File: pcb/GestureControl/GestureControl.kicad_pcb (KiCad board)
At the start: 4 copper layers, 253.9 x 54.6 mm, 177 parts, among them J1 Conn_01x04_I2I-LCD, J10 EXTERN I2C, J11 Conn_01x02, J12 Conn_01x02, J13 WR-MM Female SMT Connector, J14 WR-MM Female SMT Connector, J15 WR-MM Female SMT Connector, J16 WR-MM Female SMT Connector, J17 Conn_01x01, J18 Conn_01x01, J19 Conn_01x01, J2 BATT, J20 WR-MM Female SMT Connector, J21 WR-MM Female SMT Connector, J22 WR-MM Female SMT Connector, J23 WR-MM Female SMT Connector, J3 Conn_01x08, J4 Conn_01x06, J5 Conn_01x10, J6 Conn_01x08, J7 FTDI, J8 Conn_01x06, J9 UART, SW1 SW1, SW2 SW2, U1 AP5100_3.3, U2 AP5100_3.3, U3 VL53L3CXV0DH_1, U4 VL53L3CXV0DH_1, U5 VL53L3CXV0DH_1, U6 STM32L151RETx, U7 STM32F401RETx, U8 VL53L3CXV0DH_1, U9 VL53L3CXV0DH_1, Y1 8MHz, Y2 32kHz

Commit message: small change
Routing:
- net GND: track 427.3 -> 424.8 mm
- net +5V: track 112.6 -> 112.1 mm
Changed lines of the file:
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@@
     (effects (font (size 1 1) (thickness 0.2)) (justify left))
   )
-  (gr_text "I2C LCD" (at 40.132 96.774) (layer "F.SilkS")
+  (gr_text "I2C LCD" (at 38.1 96.774) (layer "F.SilkS")
     (effects (font (size 1 1) (thickness 0.2)))
   )
@@
     (effects (font (size 1 1) (thickness 0.2)) (justify left))
   )
-  (gr_text "FTDI" (at 41.656 88.9) (layer "F.SilkS")
+  (gr_text "FTDI" (at 42.799 86.741) (layer "F.SilkS")
     (effects (font (size 1 1) (thickness 0.2)))
   )
@@
   (segment (start 117.856 91.694) (end 116.332 91.694) (width 1) (layer "B.Cu") (net 1))
   (segment (start 104.648 88.809) (end 104.648 90.73292) (width 0.25) (layer "B.Cu") (net 1))
-  (segment (start 60.06549 88.38649) (end 58.28749 88.38649) (width 0.25) (layer "B.Cu") (net 1))
   (segment (start 68.99849 100.57849) (end 68.95549 100.57849) (width 0.25) (layer "B.Cu") (net 1))
   (segment (start 60.06549 88.38649) (end 60.06549 87.24349) (width 0.25) (layer "B.Cu") (net 1))
@@
   (segment (start 215.392 98.425) (end 214.122 98.425) (width 0.25) (layer "B.Cu") (net 1))
   (segment (start 132.588 92.379) (end 134.0565 92.379) (width 1) (layer "B.Cu") (net 1))
-  (segment (start 58.28749 88.38649) (end 57.77949 88.89449) (width 0.25) (layer "B.Cu") (net 1))
   (segment (start 253.492 98.425) (end 253.492 97.331) (width 0.25) (layer "B.Cu") (net 1))
   (segment (start 255.107 102.906) (end 256.413 102.906) (width 0.5) (layer "B.Cu") (net 1))
@@
   (segment (start 37.592 93.726) (end 37.592 89.535) (width 1) (layer "In2.Cu") (net 21))
   (segment (start 37.592 99.187) (end 37.592 99.314) (width 1) (layer "In2.Cu") (net 21))
-  (segment (start 37.592 93.726) (end 37.592 93.218) (width 1) (layer "In2.Cu") (net 21))
   (segment (start 37.592 98.425) (end 38.354 98.425) (width 1) (layer "In2.Cu") (net 21))
   (segment (start 54.584489 125.501511) (end 56.134 123.952) (width 1) (layer "In2.Cu") (net 21))
@@
   (segment (start 110.454717 107.097) (end 109.728 107.097) (width 0.25) (layer "B.Cu") (net 33))
   (segment (start 43.053 79.375) (end 43.053 85.09) (width 0.25) (layer "B.Cu") (net 33))
-  (segment (start 43.053 85.09) (end 43.033501 85.109499) (width 0.25) (layer "B.Cu") (net 33))
   (segment (start 108.458 83.657) (end 108.458 93.309) (width 0.25) (layer "B.Cu") (net 33))
   (segment (start 260.223 107.533) (end 260.223 109.3978) (width 0.25) (layer "B.Cu") (net 33))
@@
   (segment (start 184.023 109.347) (end 186.944 112.268) (width 0.25) (layer "B.Cu") (net 33))
   (segment (start 108.458 108.93) (end 108.458 119.725) (width 0.25) (layer "B.Cu") (net 33))
-  (segment (start 45.244078 96.51449) (end 45.07949 96.51449) (width 0.25) (layer "B.Cu") (net 33))
   (segment (start 61.11749 93.12549) (end 61.11749 98.00249) (width 0.25) (layer "F.Cu") (net 34))
   (segment (start 43.121478 88.89449) (end 45.154467 90.927479) (width 0.25) (layer "F.Cu") (net 34))
@@
   (segment (start 52.95349 94.483488) (end 47.366488 94.483488) (width 0.25) (layer "F.Cu") (net 38))
   (segment (start 47.36549 94.48249) (end 44.31749 94.48249) (width 0.25) (layer "F.Cu") (net 38))
-  (segment (start 52.95349 94.483488) (end 52.95349 94.48249) (width 0.25) (layer "F.Cu") (net 38))
   (segment (start 57.69249 98.05049) (end 56.520492 98.05049) (width 0.25) (layer "F.Cu") (net 38))
   (segment (start 56.520492 98.05049) (end 52.95349 94.483488) (width 0.25) (layer "F.Cu") (net 38))
@@
   (segment (start 47.366488 94.483488) (end 47.36549 94.48249) (width 0.25) (layer "F.Cu") (net 38))
   (segment (start 57.69249 95.05049) (end 55.04549 95.05049) (width 0.25) (layer "F.Cu") (net 39))
-  (segment (start 52.954488 92.70449) (end 52.69949 92.70449) (width 0.25) (layer "F.Cu") (net 39))
   (segment (start 55.04549 95.05049) (end 52.69949 92.70449) (width 0.25) (layer "F.Cu") (net 39))
   (segment (start 57.651991 92.836031) (end 59.49147 94.67551) (width 0.25) (layer "F.Cu") (net 40))

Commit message: feedback verwerking philip
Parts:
- C29, R20: moved to F.Cu
- moved C7 13.1 mm to (23.7, 120.2), turned to 90 degrees
- moved D7 11.2 mm to (36.2, 118.4), turned to 90 degrees
- moved D8 10.3 mm to (27.4, 77.2), turned to 90 degrees
- moved R27 9.74 mm to (29.0, 113.3), turned to 90 degrees
- moved R18 9.39 mm to (24.6, 113.3), turned to -90 degrees
- moved R25 8.62 mm to (26.8, 113.3), turned to 90 degrees
- moved C5 7.63 mm to (33.3, 115.5), turned to 90 degrees
- moved C3 7.03 mm to (30.9, 124.0), turned to -90 degrees
- moved L1 6.55 mm to (40.9, 117.6), turned to 90 degrees
- moved C34 6.38 mm to (23.0, 75.1)
- moved R20 6.13 mm to (49.8, 99.6), turned to 0 degrees
- moved C13 5.95 mm to (37.0, 112.4)
- moved R23 5.69 mm to (33.3, 119.3), turned to 90 degrees
- moved C33 5.69 mm to (64.0, 99.1), turned to 180 degrees
- moved JP3 5.25 mm to (66.4, 95.5)
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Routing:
- net GND: track 424.8 -> 320.1 mm, vias 141 -> 154
- net +3V3: track 891.3 -> 869.4 mm, vias 49 -> 50
- net VCC: track 60.6 -> 50.0 mm
- net +5V: track 112.1 -> 101.9 mm, vias 5 -> 4
- net /STM32L151RET6TR/FTDI_RTS: track 33.8 -> 24.3 mm, vias 2 -> 0
- net /STM32L151RET6TR/PIN30: track 10.4 -> 2.85 mm
- net BUCK_5_EN: track 55.2 -> 48.8 mm
- net XSHUT_4: track 276.1 -> 273.3 mm
- net SDA2: track 39.3 -> 36.6 mm
- net /STM32L151RET6TR/PIN41: track 3.95 -> 6.63 mm
- net GPIOI_3: track 282.0 -> 284.3 mm
- net LED_1: track 54.9 -> 52.7 mm
- net BUCK_33_EN: track 1.98 -> 3.07 mm
- net LED_3: track 41.3 -> 40.4 mm
- net XSHUT_0: track 95.3 -> 94.4 mm
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- removed copper zone on In2.Cu, net +5V
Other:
- outline, holes or cut-outs redrawn

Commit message: feedback verwerling philip
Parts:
- C1, C2, R8, R9: moved to F.Cu
- moved R18 15.6 mm to (40.1, 115.0), turned to 180 degrees
- moved C13 15.3 mm to (23.5, 119.7), turned to 90 degrees
- moved R25 13.3 mm to (40.1, 113.0), turned to 0 degrees
- moved R8 12.7 mm to (89.5, 86.0)
- moved R14 11.9 mm to (30.5, 111.6), turned to 0 degrees
- moved L1 11.8 mm to (30.2, 122.6), turned to 180 degrees
- moved R27 11.4 mm to (40.1, 111.0), turned to 0 degrees
- moved C7 10.8 mm to (25.0, 109.5), turned to 180 degrees
- moved R6 10.4 mm to (88.7, 82.9), turned to 180 degrees
- moved C3 10.3 mm to (27.1, 114.4), turned to 180 degrees
- moved C1 8.75 mm to (87.6, 85.8)
- moved D7 6.80 mm to (29.4, 118.0), turned to 180 degrees
- moved R7 6.63 mm to (71.3, 82.9)
- moved U1 5.05 mm to (33.6, 114.4), turned to 180 degrees
- moved C5 4.40 mm to (37.4, 117.0)
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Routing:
- net VCC: track 50.0 -> 42.2 mm, vias 8 -> 0
- net +3V3: track 869.4 -> 873.5 mm, vias 50 -> 55
- net /OUT3.3: track 0.00 -> 2.70 mm
- net +5V: track 101.9 -> 99.4 mm, vias 4 -> 7
- net SW_2: track 69.3 -> 71.7 mm
- net Net-(D6-Pad2): track 4.86 -> 7.21 mm
- net GPIOI_3: track 284.3 -> 282.0 mm, vias 9 -> 7
- net SW_1: track 77.1 -> 78.6 mm
- net Net-(R25-Pad1): track 4.59 -> 5.67 mm
- net GPIOI_2: track 192.2 -> 191.2 mm
- net BUCK_33_EN: track 3.07 -> 2.01 mm
- net LED_1: track 52.7 -> 51.7 mm
- net GPIOI_1: track 142.6 -> 141.6 mm, vias 6 -> 5
- net LED_3: track 40.4 -> 39.6 mm
- net GPIOI_0: track 83.0 -> 83.8 mm
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- added copper zone on B.Cu, net GND
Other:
- board text added: "1"
- board text added: "2"
- board text added: "3"
- board text added: "4"

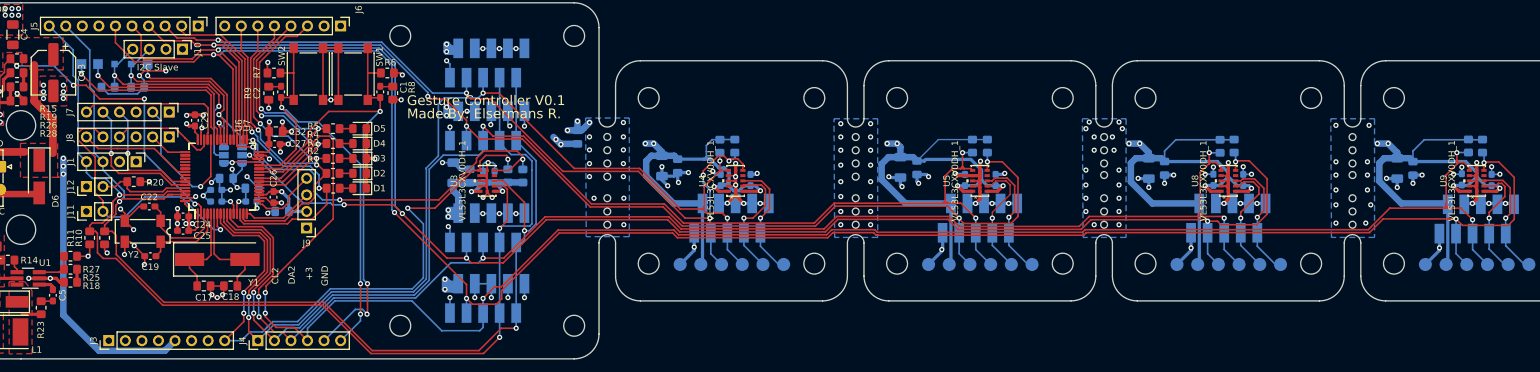
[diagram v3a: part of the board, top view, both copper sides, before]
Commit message: add vias
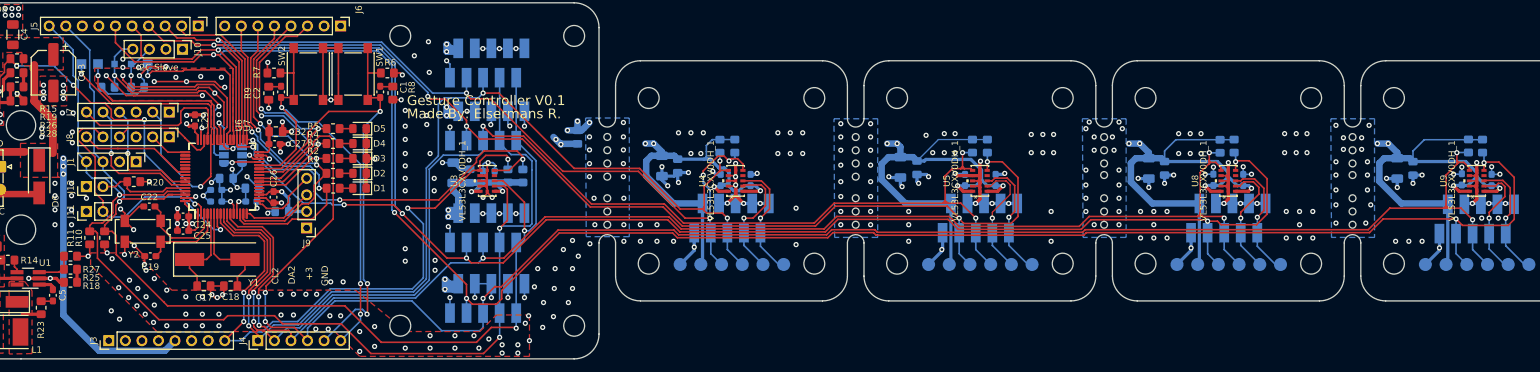
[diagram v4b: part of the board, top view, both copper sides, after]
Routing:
- net GND: track 319.4 -> 378.5 mm, vias 203 -> 393
- net /STM32L151RET6TR/PC8: track 22.1 -> 25.2 mm
- net /STM32L151RET6TR/FTDI_RTS: track 24.3 -> 26.4 mm
- net XSHUT_3: track 208.9 -> 210.3 mm
- net SDA2: track 36.6 -> 35.1 mm
- net BUCK_5_EN: track 48.8 -> 47.7 mm
- net /STM32L151RET6TR/PA10: track 29.8 -> 28.7 mm
- net SCL1: track 421.6 -> 422.6 mm
- net XSHUT_2: track 191.8 -> 192.4 mm
- added copper zone on In2.Cu, net GND

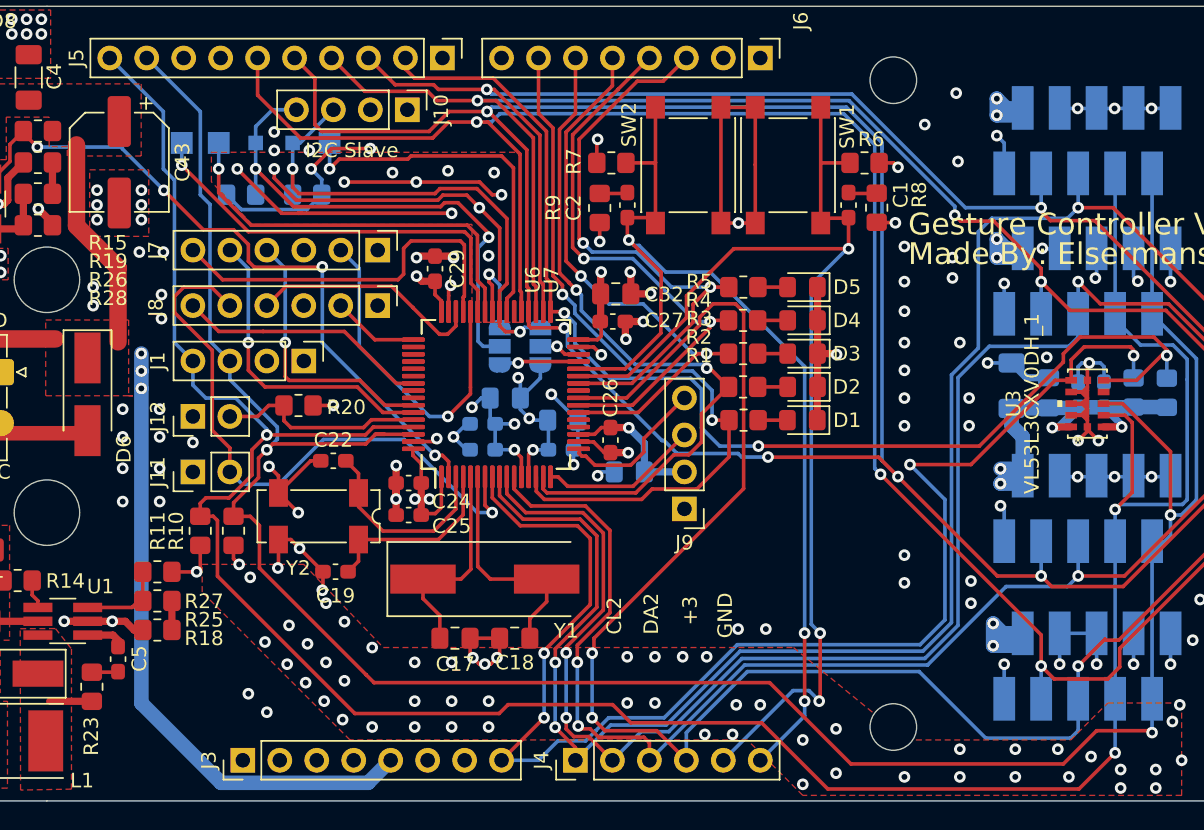
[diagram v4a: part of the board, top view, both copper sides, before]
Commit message: ADD RC op I2C
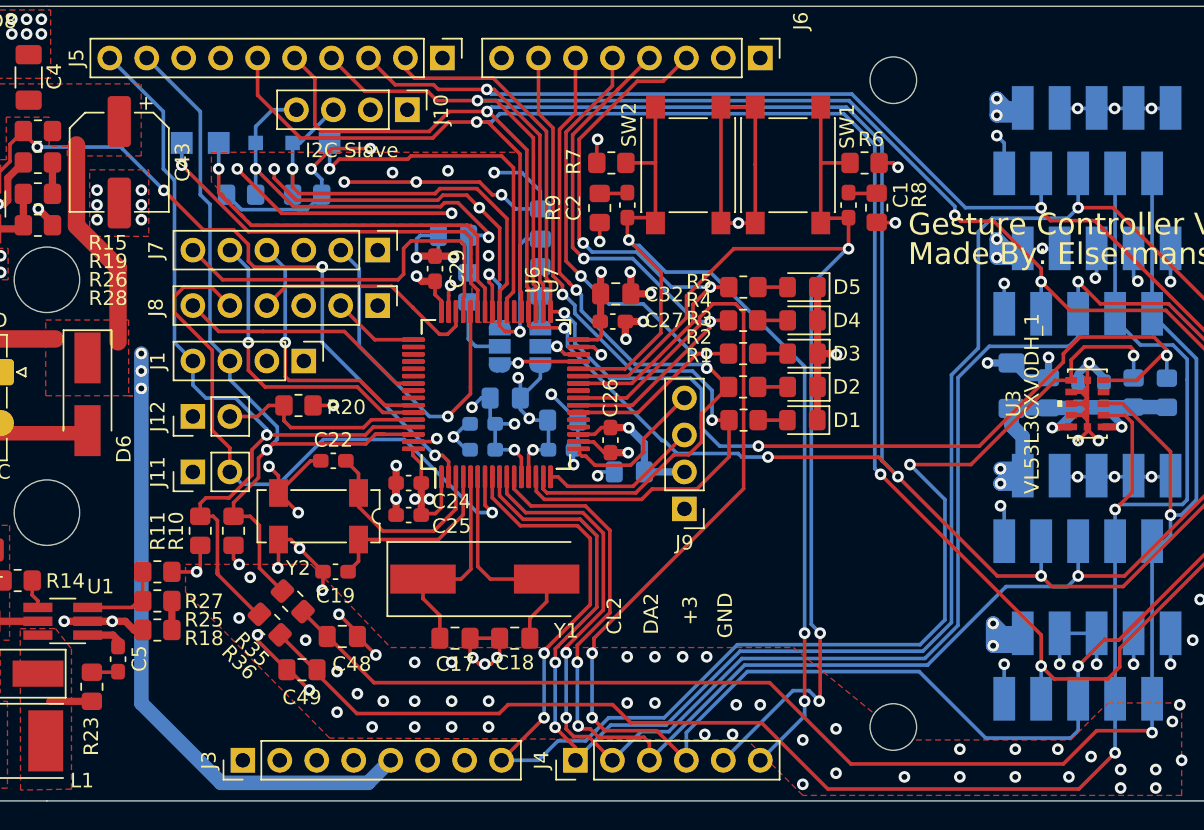
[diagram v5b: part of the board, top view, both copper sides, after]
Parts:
- added C48: x, Capacitor_SMD:C_0805_2012Metric_Pad1.18x1.45mm_HandSolder, F.Cu at (52.8, 115.4)
- added C49: x, Capacitor_SMD:C_0805_2012Metric_Pad1.18x1.45mm_HandSolder, F.Cu at (50.0, 117.7)
- added C50: x, Capacitor_SMD:C_0805_2012Metric_Pad1.18x1.45mm_HandSolder, B.Cu at (66.4, 87.1)
- added C51: x, Capacitor_SMD:C_0805_2012Metric_Pad1.18x1.45mm_HandSolder, B.Cu at (60.5, 87.9)
- added R35: x, Resistor_SMD:R_0805_2012Metric_Pad1.20x1.40mm_HandSolder, F.Cu at (49.4, 113.0)
- added R36: x, Resistor_SMD:R_0805_2012Metric_Pad1.20x1.40mm_HandSolder, F.Cu at (47.8, 114.6)
- added R37: x, Resistor_SMD:R_0805_2012Metric_Pad1.20x1.40mm_HandSolder, B.Cu at (66.4, 91.0)
- added R38: x, Resistor_SMD:R_0805_2012Metric_Pad1.20x1.40mm_HandSolder, B.Cu at (61.5, 91.5)
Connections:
- J6 pad 3: LED_5 -> LED_4
- J6 pad 4: LED_4 -> LED_3
- J6 pad 5: LED_3 -> LED_2
- J6 pad 6: LED_2 -> LED_1
- J6 pad 7: LED_1 -> LED_0
- R1 pad 2: LED_1 -> LED_0
- R2 pad 2: LED_2 -> LED_1
- R3 pad 2: LED_3 -> LED_2
- R4 pad 2: LED_4 -> LED_3
- R5 pad 2: LED_5 -> LED_4
- U6 pad 14: LED_1 -> LED_0
- U6 pad 15: LED_2 -> LED_1
- U6 pad 22: LED_3 -> LED_2
- U6 pad 23: LED_4 -> LED_3
- U6 pad 26: LED_5 -> LED_4
- U7 pad 14: LED_1 -> LED_0
- U7 pad 15: LED_2 -> LED_1
- U7 pad 22: LED_3 -> LED_2
- U7 pad 23: LED_4 -> LED_3
- U7 pad 26: LED_5 -> LED_4
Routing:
- net LED_0: track 0.00 -> 51.7 mm, vias 0 -> 2
- net LED_5: track 40.7 -> 0.00 mm, vias 2 -> 0
- net GND: track 378.5 -> 401.5 mm, vias 393 -> 350
- net SDA2: track 35.1 -> 45.2 mm
- net LED_2: track 48.6 -> 39.6 mm
- net LED_1: track 51.7 -> 48.6 mm
- net SDA1: track 413.4 -> 411.4 mm
- net SCL1: track 422.6 -> 421.0 mm
- net LED_4: track 39.7 -> 40.7 mm
- net +3V3: track 873.8 -> 872.9 mm

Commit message: add PCBV0.23
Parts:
- added ?: , , F.Cu at (236.7, 96.8)
- added ?: , , F.Cu at (122.4, 96.8)
- added ?: , , F.Cu at (236.7, 106.2)
- added ?: , , F.Cu at (122.4, 94.7)
- added ?: , , F.Cu at (122.4, 104.1)
- added ?: , , F.Cu at (198.6, 92.7)
- added ?: , , F.Cu at (160.5, 102.1)
- added ?: , , F.Cu at (236.7, 94.7)
- added ?: , , F.Cu at (236.7, 104.1)
- added ?: , , F.Cu at (198.6, 106.2)
- added ?: , , F.Cu at (198.6, 104.1)
- added ?: , , F.Cu at (160.5, 94.7)
- added ?: , , F.Cu at (160.5, 104.1)
- added ?: , , F.Cu at (122.4, 106.2)
- added ?: , , F.Cu at (160.5, 96.8)
- added ?: , , F.Cu at (122.4, 92.7)
- added ?: , , F.Cu at (160.5, 92.7)
- added ?: , , F.Cu at (160.5, 106.2)
- added ?: , , F.Cu at (236.7, 102.1)
- added ?: , , F.Cu at (198.6, 99.4)
- added ?: , , F.Cu at (236.7, 92.7)
- added ?: , , F.Cu at (122.4, 99.4)
- added ?: , , F.Cu at (198.6, 94.7)
- added ?: , , F.Cu at (122.4, 102.1)
- added ?: , , F.Cu at (198.6, 102.1)
- added ?: , , F.Cu at (160.5, 99.4)
- added ?: , , F.Cu at (236.7, 99.6)
- added ?: , , F.Cu at (198.6, 96.8)
- added REF**: coördinatiepunt, coördinatiePunt:coördinatiepunt, F.Cu at (267.1, 75.0)
- added REF**: coördinatiepunt, coördinatiePunt:coördinatiepunt, B.Cu at (198.6, 75.0)
- added REF**: coördinatiepunt, coördinatiePunt:coördinatiepunt, F.Cu at (87.1, 109.5)
- added REF**: coördinatiepunt, coördinatiePunt:coördinatiepunt, F.Cu at (255.9, 123.6)
- added REF**: coördinatiepunt, coördinatiePunt:coördinatiepunt, F.Cu at (127.4, 75.0)
- added REF**: coördinatiepunt, coördinatiePunt:coördinatiepunt, B.Cu at (127.3, 123.6)
- added REF**: coördinatiepunt, coördinatiePunt:coördinatiepunt, B.Cu at (78.0, 112.1)
- added REF**: coördinatiepunt, coördinatiePunt:coördinatiepunt, B.Cu at (233.3, 123.6)
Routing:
- net VCC: track 42.2 -> 13.2 mm
- net GND: track 401.5 -> 388.4 mm, vias 350 -> 433
- net XSHUT_3: track 210.3 -> 220.5 mm
- net /STM32L151RET6TR/FTDI_CTS: track 23.1 -> 13.8 mm
- net Net-(D6-Pad2): track 7.21 -> 0.00 mm
- net XSHUT_4: track 274.1 -> 280.6 mm
- net GPIOI_3: track 282.0 -> 288.2 mm
- net XSHUT_2: track 192.4 -> 196.4 mm
- net SW_2: track 71.7 -> 75.1 mm
- net SW_1: track 78.6 -> 81.8 mm
- net GPIOI_2: track 191.2 -> 194.3 mm
- net SDA1: track 411.4 -> 413.2 mm
- net GPIOI_4: track 296.8 -> 298.1 mm
- net XSHUT_1: track 159.2 -> 160.4 mm
- net GPIOI_1: track 141.6 -> 142.7 mm
- added copper zone on F.Cu, net Net-(D6-Pad2)
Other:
- board size 253.9 x 54.6 mm -> 254.1 x 68.7 mm
- board text added: "Gesture Controller V0.22"
- board text removed: "Gesture Controller V0.1"

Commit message: add PCBV0.3
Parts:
- removed J3, J6: Conn_01x08, Connector_PinHeader_2.54mm:PinHeader_1x08_P2.54mm_Vertical
- removed J4: Conn_01x06, Connector_PinHeader_2.54mm:PinHeader_1x06_P2.54mm_Vertical
- removed J5: Conn_01x10, Connector_PinHeader_2.54mm:PinHeader_1x10_P2.54mm_Vertical
- added J24: Conn_02x19_Odd_Even, Connector_PinSocket_2.54mm:PinSocket_2x19_P2.54mm_Vertical, B.Cu at (36.1, 131.3)
- added J25: Conn_02x19_Odd_Even, Connector_PinSocket_2.54mm:PinSocket_2x19_P2.54mm_Vertical, B.Cu at (36.1, 70.4)
- moved C5 6.02 mm to (37.2, 123.0)
- moved C7 6.02 mm to (24.8, 115.5)
- moved D7 6.02 mm to (29.2, 124.0)
- moved L1 6.02 mm to (30.0, 128.6)
- moved R14 6.02 mm to (30.3, 117.6)
- moved R18 6.02 mm to (39.9, 121.0)
- moved R25 6.02 mm to (39.9, 119.0)
- moved R27 6.02 mm to (39.9, 117.0)
- moved C13 6.02 mm to (23.3, 125.7)
- moved C3 6.02 mm to (26.9, 120.4)
- moved R23 6.02 mm to (35.4, 124.9)
- moved U1 6.02 mm to (33.4, 120.4)
- moved C34 4.25 mm to (23.0, 70.8)
- moved C6 4.25 mm to (24.4, 82.7)
- moved D8 4.25 mm to (27.4, 72.9)
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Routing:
- net XSHUT_0: track 94.6 -> 129.9 mm, vias 4 -> 5
- net GPIOI_0: track 83.9 -> 113.4 mm, vias 3 -> 4
- net LED_3: track 39.8 -> 65.1 mm
- net SCL2: track 35.2 -> 58.0 mm, vias 2 -> 3
- net SDA2: track 45.2 -> 65.0 mm
- net +5V: track 99.4 -> 108.7 mm
- net +3V3: track 872.9 -> 881.4 mm, vias 55 -> 56
- net XSHUT_3: track 220.5 -> 228.8 mm
- net XSHUT_2: track 196.4 -> 204.3 mm
- net XSHUT_4: track 280.6 -> 288.5 mm
- net XSHUT_1: track 160.4 -> 167.9 mm
- net LED_2: track 39.7 -> 45.1 mm
- net LED_1: track 48.6 -> 54.0 mm
- net LED_0: track 51.6 -> 56.8 mm
- net GPIOI_3: track 288.2 -> 283.2 mm
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- added copper zone on F.Cu, net (none)
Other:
- board size 254.1 x 68.7 mm -> 254.1 x 81.6 mm
- board text added: "Gesture Controller V0.3"
- board text removed: "G0"
- board text removed: "G2"
- board text removed: "G3"
- board text removed: "G4"
- board text removed: "Gesture Controller V0.22"
- board text removed: "SW1"
- board text removed: "SW2"
- board text removed: "XS0"
- board text removed: "XS2"
- board text removed: "XS3"
- board text removed: "XS4"
